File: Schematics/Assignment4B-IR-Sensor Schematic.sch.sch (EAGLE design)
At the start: 7 parts, among them U1 BS170

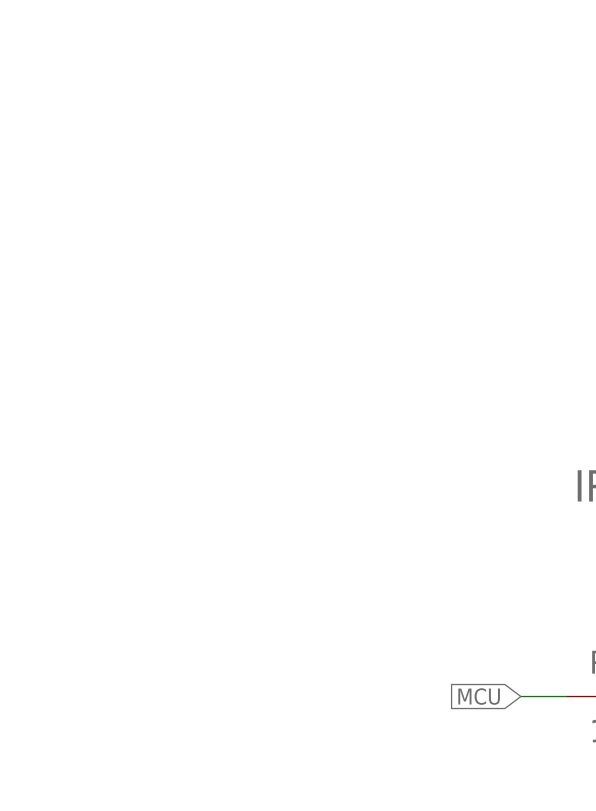
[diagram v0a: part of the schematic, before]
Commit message: Updated 4B schematic and added IR receiver circuit
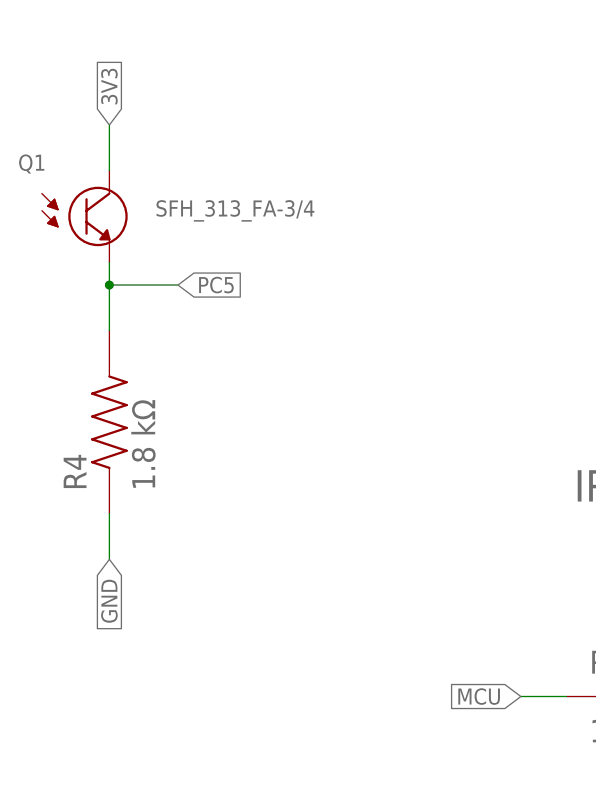
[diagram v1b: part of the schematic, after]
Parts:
- added Q1: SFH_313_FA-3/4, SFH_313_FA-3_4:SFH_313_FA-3/4
- added R4: 1.8 kΩ, CRCW08051K80FKEB:CRCW08051K80FKEB
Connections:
- new net PC5: Q1.E, R4.2
- net 3V3: now also Q1.C
- net GND: now also R4.1
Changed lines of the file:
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@@
 <part name="R1" library="CRCW080551R0FKEAHP" deviceset="CRCW080551R0FKEAHP" device="" value="51 Ω "/>
 <part name="R3" library="CRCW080547K0JNEA" deviceset="CRCW080547K0JNEA" device="" value="47 kΩ "/>
+<part name="R4" library="CRCW08051K80FKEB" deviceset="CRCW08051K80FKEB" device="" value="1.8 kΩ"/>
+<part name="Q1" library="SFH_313_FA-3_4" deviceset="SFH_313_FA-3/4" device=""/>
 </parts>
 <sheets>
@@
 <attribute name="NAME" x="45.71851875" y="20.315559375" size="2.54148125" layer="95" rot="R90"/>
 <attribute name="VALUE" x="53.346640625" y="20.31003125" size="2.54331875" layer="96" rot="R90"/>
+</instance>
+<instance part="R4" gate="G$1" x="-27.94" y="76.2" smashed="yes" rot="R90">
+<attribute name="NAME" x="-30.48148125" y="68.575559375" size="2.54148125" layer="95" rot="R90"/>
+<attribute name="VALUE" x="-22.853359375" y="68.57003125" size="2.54331875" layer="96" rot="R90"/>
+</instance>
+<instance part="Q1" gate="G$1" x="-30.48" y="99.06" smashed="yes">
+<attribute name="NAME" x="-38.0956" y="104.1422" size="1.779540625" layer="95"/>
+<attribute name="VALUE" x="-22.8508" y="99.06" size="1.78121875" layer="96"/>
 </instance>
 </instances>
@@
 <label x="55.88" y="7.62" size="1.778" layer="95" rot="R270" xref="yes"/>
 </segment>
+<segment>
+<pinref part="R4" gate="G$1" pin="1"/>
+<wire x1="-27.94" y1="66.04" x2="-27.94" y2="60.96" width="0.1524" layer="91"/>
+<label x="-27.94" y="60.96" size="1.778" layer="95" rot="R270" xref="yes"/>
+</segment>
 </net>
 <net name="N$3" class="0">
@@
 <label x="55.88" y="111.76" size="1.778" layer="95" rot="R90" xref="yes"/>
 </segment>
+<segment>
+<pinref part="Q1" gate="G$1" pin="C"/>
+<wire x1="-27.94" y1="104.14" x2="-27.94" y2="109.22" width="0.1524" layer="91"/>
+<label x="-27.94" y="109.22" size="1.778" layer="95" rot="R90" xref="yes"/>
+</segment>
 </net>
+<net name="PC5" class="0">
+<segment>
+<pinref part="R4" gate="G$1" pin="2"/>
+<wire x1="-27.94" y1="86.36" x2="-27.94" y2="91.44" width="0.1524" layer="91"/>
+<wire x1="-27.94" y1="91.44" x2="-27.94" y2="93.98" width="0.1524" layer="91"/>
+<wire x1="-27.94" y1="91.44" x2="-20.32" y2="91.44" width="0.1524" layer="91"/>
+<junction x="-27.94" y="91.44"/>
+<pinref part="Q1" gate="G$1" pin="E"/>
+<label x="-20.32" y="91.44" size="1.778" layer="95" xref="yes"/>
+</segment>
+</net>
